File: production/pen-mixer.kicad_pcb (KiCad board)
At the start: 4 copper layers, 11 x 42 mm, 32 parts, among them J1 USB-C 16P, J2 BAT, J3 FSR, U1 ISP1807-LR, U2 LSM6DSV16X, U3 MCP73831T-2ACI/OT, U4 TPS7A0233DQN

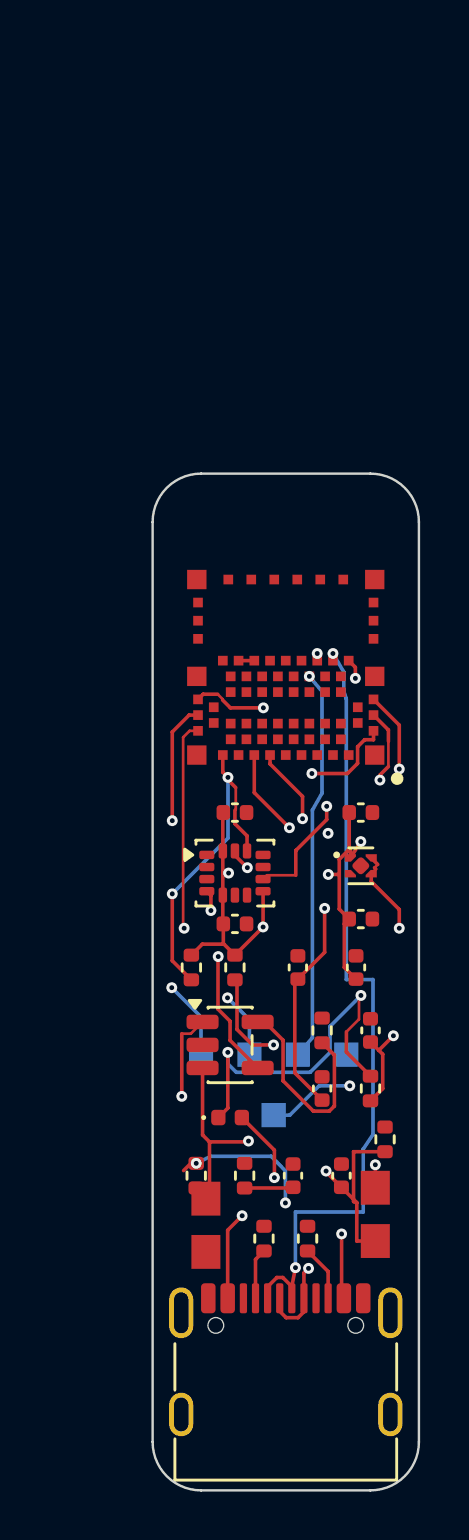
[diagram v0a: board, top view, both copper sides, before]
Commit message: vendor footprint full track routing
Claude-Session: https://claude.ai/code/session_01RCYT2QSY7BVZDeTyE9KrC4
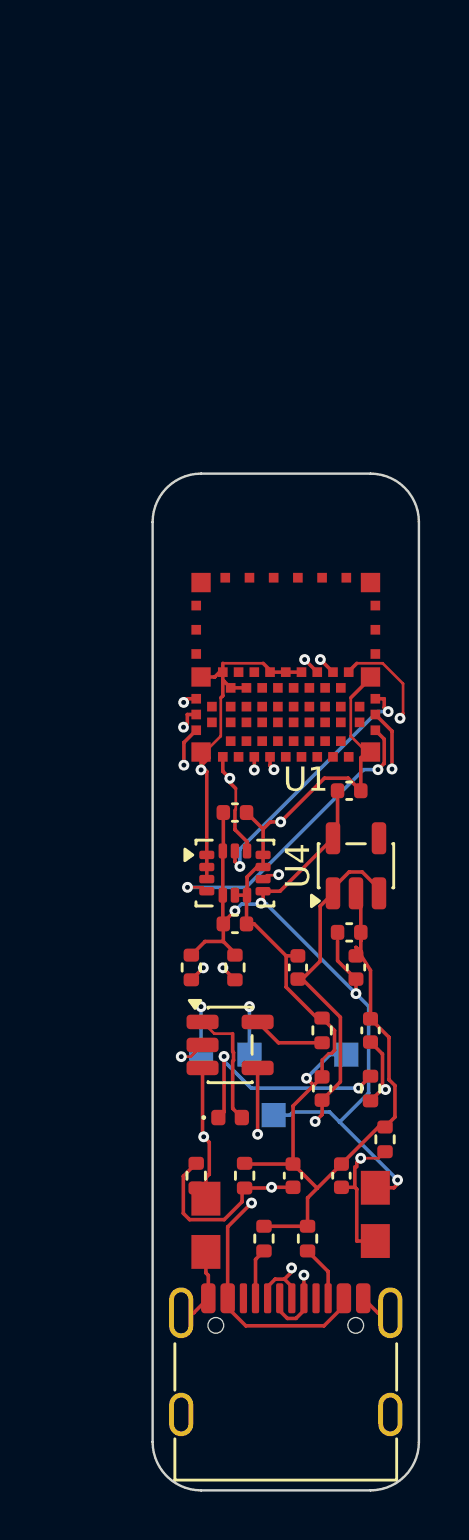
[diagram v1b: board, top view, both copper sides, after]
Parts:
- removed TP3: nRESET, TestPad_1.0mm
- U1: footprint ISP1807_LGA78_8x8mm -> ISP1807-LR
- U4: value TPS7A0233DQN -> TPS7A0533PDBV; footprint Texas_X2SON-4_1x1mm_P0.65mm -> SOT-23-5
- moved U1 5.66 mm to (109.5, 72.0)
- moved C5 1.02 mm to (108.1, 73.1)
- moved C6 0.73 mm to (108.1, 79.0)
- moved U4 0.20 mm to (108.4, 76.2), turned to 90 degrees
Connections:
- U1 pad 13: nRESET -> (no net)
- U1 pad 20: ANT -> (no net)
- U1 pad 22: ANT -> (no net)
- U4 pad 1: +3V3 -> VBAT
- U4 pad 4: VBAT -> (no net)
- U4 pad 5: GND -> +3V3
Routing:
- net GND: track 0.00 -> 112.4 mm, vias 1 -> 4
- net +3V3: track 27.8 -> 49.8 mm, vias 7 -> 5
- net nRESET: track 16.1 -> 0.00 mm, vias 1 -> 0
- net VBAT_SENSE: track 12.6 -> 25.8 mm, vias 3 -> 2
- net VBAT: track 34.5 -> 24.9 mm, vias 3 -> 2
- net VBUS: track 57.1 -> 48.7 mm, vias 5 -> 4
- net SCL: track 24.1 -> 16.2 mm
- net CHG_STAT: track 11.9 -> 5.10 mm, vias 2 -> 0
- net IPROG: track 8.59 -> 3.02 mm
- net LED_A: track 15.0 -> 9.53 mm
- net USB_DM: track 32.9 -> 29.3 mm
- net USB_DP: track 29.6 -> 32.1 mm
- net FSR_SENSE: track 27.9 -> 25.9 mm
- net IMU_INT2: track 10.5 -> 9.75 mm
- net SDA: track 14.0 -> 13.3 mm
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
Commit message: stock symbols full route zero unrouted
Claude-Session: https://claude.ai/code/session_01RCYT2QSY7BVZDeTyE9KrC4
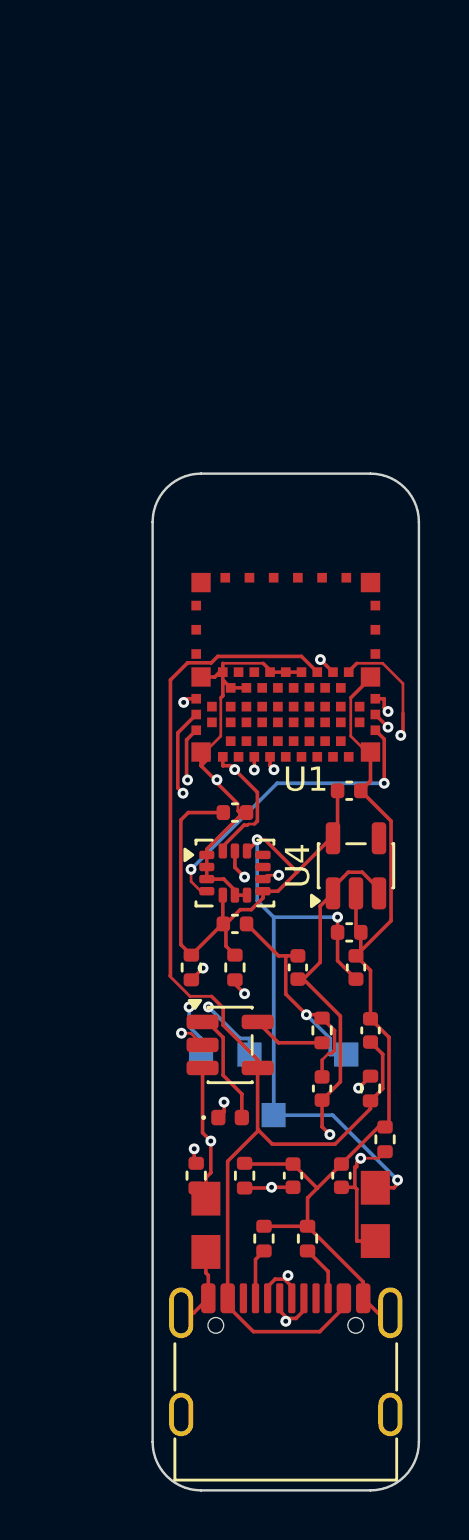
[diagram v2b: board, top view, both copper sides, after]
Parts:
- U2: value LSM6DSV16X -> LSM6DS3TR-C
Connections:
- U2 pad 10: GND -> (no net)
- U2 pad 11: GND -> (no net)
- U2 pad 12: SDA -> +3V3
- U2 pad 14: +3V3 -> SDA
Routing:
- net GND: track 112.4 -> 120.0 mm, vias 4 -> 3
- net +3V3: track 49.8 -> 55.9 mm, vias 5 -> 4
- net LED_A: track 9.53 -> 7.23 mm
- net VBAT_SENSE: track 25.8 -> 24.1 mm, vias 2 -> 3
- net SDA: track 13.3 -> 14.9 mm
- net USB_DP: track 32.1 -> 33.5 mm
- net VBUS: track 48.7 -> 49.8 mm, vias 4 -> 0
- net VBAT: track 24.9 -> 25.8 mm
- net SCL: track 16.2 -> 17.1 mm
- net SWDCLK: track 14.7 -> 15.3 mm

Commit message: remove fsr rearrange back pads
Claude-Session: https://claude.ai/code/session_01RCYT2QSY7BVZDeTyE9KrC4
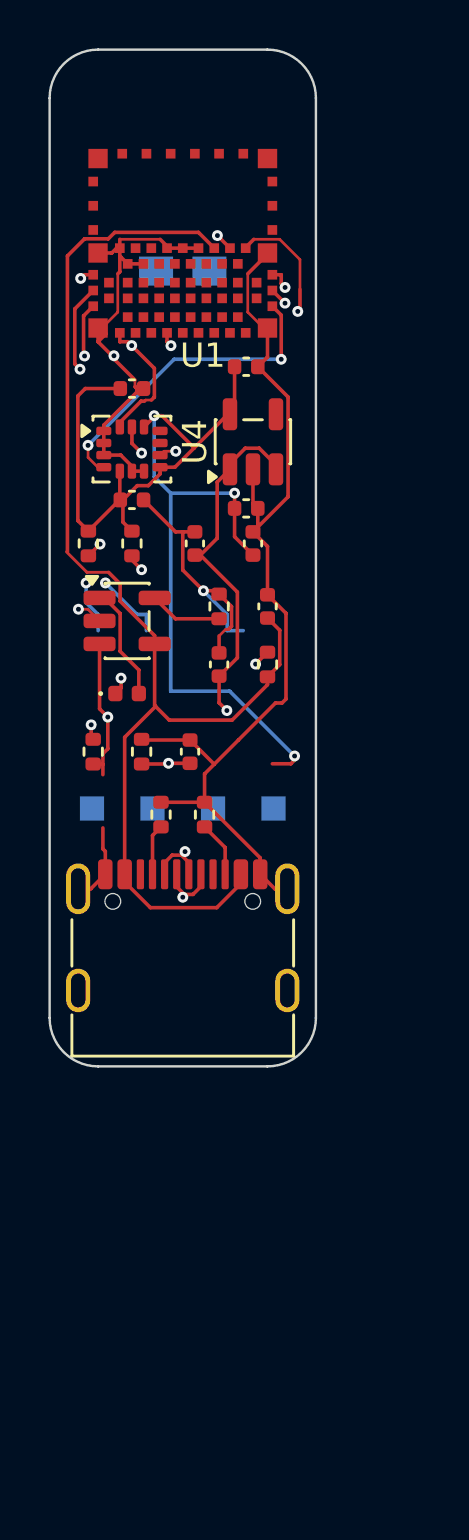
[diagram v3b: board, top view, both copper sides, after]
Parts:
- removed C9: 100n, C_0402_1005Metric
- removed J3: FSR, SolderPad_1.2x2.0mm
- removed R5: 10k, R_0402_1005Metric
- J2: moved to B.Cu
- moved J2 39.4 mm to (101.2, 51.6), turned to 90 degrees
- moved C2 18.0 mm to (102.7, 67.9)
- moved C3 18.0 mm to (101.7, 62.9)
- moved C4 18.0 mm to (104.1, 62.9)
- moved J1 18.0 mm to (101.2, 80.3)
- moved R4 18.0 mm to (104.7, 67.9)
- moved R7 18.0 mm to (99.1, 62.9)
- moved R6 18.0 mm to (97.3, 62.9)
- moved C6 18.0 mm to (103.9, 61.4)
- moved C7 18.0 mm to (99.1, 56.5)
- moved U1 18.0 mm to (105.2, 54.5)
- moved U2 18.0 mm to (99.1, 59.0)
- moved U4 18.0 mm to (104.1, 58.7)
- moved C1 18.0 mm to (104.7, 65.5)
- moved C10 18.0 mm to (101.5, 71.5)
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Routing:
- net FSR_SENSE: track 25.6 -> 0.00 mm, vias 2 -> 0

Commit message: swap tp and battery pad ends
Claude-Session: https://claude.ai/code/session_01RCYT2QSY7BVZDeTyE9KrC4
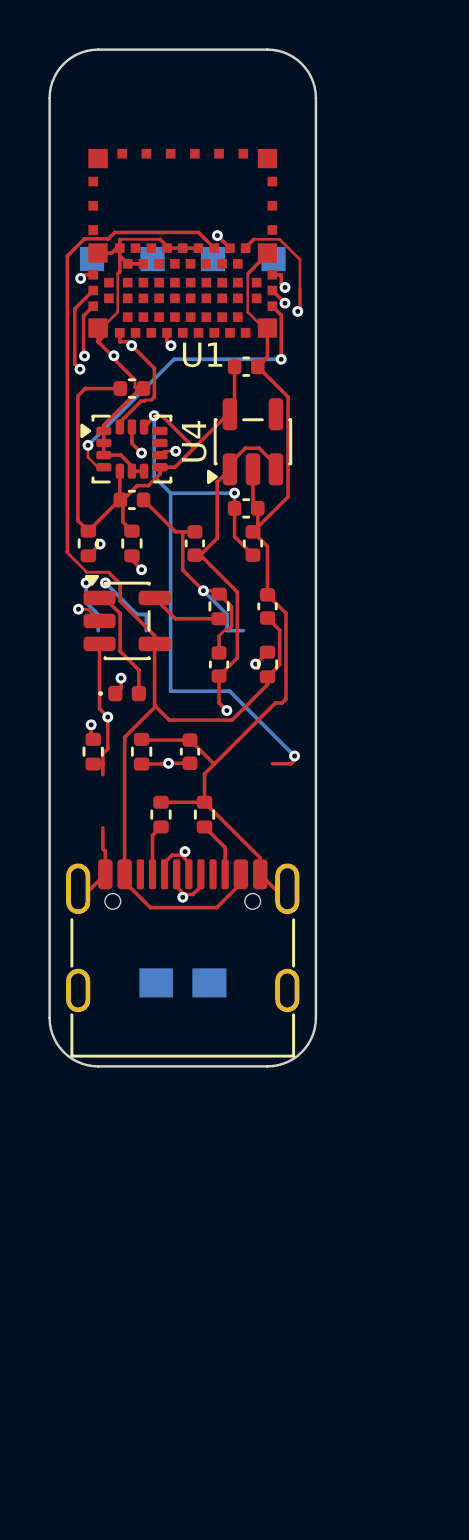
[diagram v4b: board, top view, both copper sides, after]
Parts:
- moved J2 29.4 mm to (101.2, 81.0)
- moved TP1 22.7 mm to (97.5, 51.1)
- moved TP2 22.7 mm to (100.0, 51.1)
- moved TP4 22.7 mm to (102.5, 51.1)
- moved TP5 22.7 mm to (105.0, 51.1)
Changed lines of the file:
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@@
 	(footprint "TestPad_1.0mm"
 		(layer "B.Cu")
-		(at 99.9952 73.8352)
+		(at 99.9952 51.1352)
 		(descr "1.0mm round-ish pogo test pad")
 		(property "Reference" "TP2"
@@
 	(footprint "TestPad_1.0mm"
 		(layer "B.Cu")
-		(at 104.9952 73.8352)
+		(at 104.9952 51.1352)
 		(descr "1.0mm round-ish pogo test pad")
 		(property "Reference" "TP5"
@@
 	(footprint "TestPad_1.0mm"
 		(layer "B.Cu")
-		(at 102.4952 73.8352)
+		(at 102.4952 51.1352)
 		(descr "1.0mm round-ish pogo test pad")
 		(property "Reference" "TP4"
@@
 	(footprint "SolderPad_1.2x2.0mm"
 		(layer "B.Cu")
-		(at 101.2452 51.6352 90)
+		(at 101.2452 81.0352 90)
 		(descr "Wire solder pad pair, 2.0mm pitch")
 		(property "Reference" "J2"
@@
 	(footprint "TestPad_1.0mm"
 		(layer "B.Cu")
-		(at 97.4952 73.8352)
+		(at 97.4952 51.1352)
 		(descr "1.0mm round-ish pogo test pad")
 		(property "Reference" "TP1"

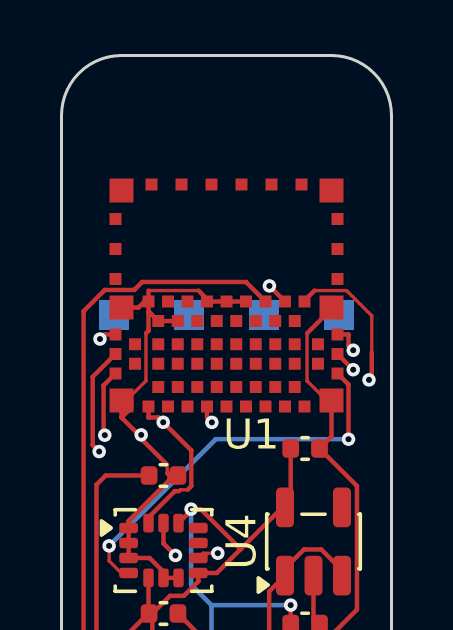
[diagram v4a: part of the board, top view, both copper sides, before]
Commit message: nudge tp1 clear of via
Claude-Session: https://claude.ai/code/session_01RCYT2QSY7BVZDeTyE9KrC4
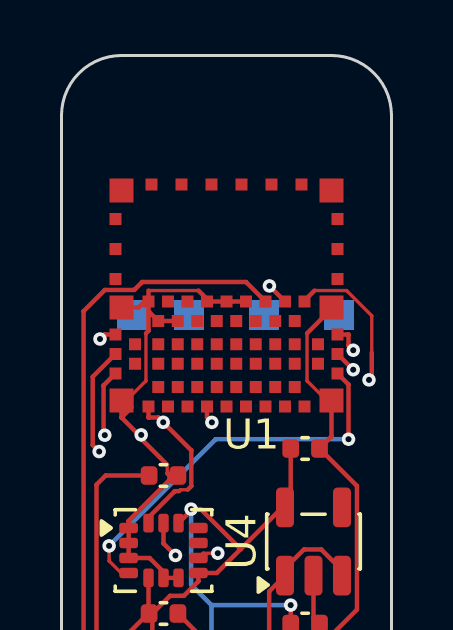
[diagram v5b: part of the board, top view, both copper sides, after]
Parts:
- moved TP1 0.60 mm to (98.1, 51.1)
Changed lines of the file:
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@@
 	(footprint "TestPad_1.0mm"
 		(layer "B.Cu")
-		(at 97.4952 51.1352)
+		(at 98.0952 51.1352)
 		(descr "1.0mm round-ish pogo test pad")
 		(property "Reference" "TP1"

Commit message: pads to board extremes
Claude-Session: https://claude.ai/code/session_01RCYT2QSY7BVZDeTyE9KrC4
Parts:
- moved J2 2.40 mm to (101.2, 83.4)
- moved TP5 1.49 mm to (103.9, 50.1)
- moved TP4 1.28 mm to (101.7, 50.1)
- moved TP1 1.08 mm to (97.7, 50.1)
- moved TP2 1.00 mm to (99.9, 50.1)
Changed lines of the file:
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@@
 	(footprint "TestPad_1.0mm"
 		(layer "B.Cu")
-		(at 99.9952 51.1352)
+		(at 99.8952 50.1352)
 		(descr "1.0mm round-ish pogo test pad")
 		(property "Reference" "TP2"
@@
 	(footprint "TestPad_1.0mm"
 		(layer "B.Cu")
-		(at 104.9952 51.1352)
+		(at 103.8952 50.1352)
 		(descr "1.0mm round-ish pogo test pad")
 		(property "Reference" "TP5"
@@
 	(footprint "TestPad_1.0mm"
 		(layer "B.Cu")
-		(at 102.4952 51.1352)
+		(at 101.6952 50.1352)
 		(descr "1.0mm round-ish pogo test pad")
 		(property "Reference" "TP4"
@@
 	(footprint "SolderPad_1.2x2.0mm"
 		(layer "B.Cu")
-		(at 101.2452 81.0352 90)
+		(at 101.2452 83.4352 90)
 		(descr "Wire solder pad pair, 2.0mm pitch")
 		(property "Reference" "J2"
@@
 	(footprint "TestPad_1.0mm"
 		(layer "B.Cu")
-		(at 98.0952 51.1352)
+		(at 97.6952 50.1352)
 		(descr "1.0mm round-ish pogo test pad")
 		(property "Reference" "TP1"

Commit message: test pads to board tip
Claude-Session: https://claude.ai/code/session_01RCYT2QSY7BVZDeTyE9KrC4
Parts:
- moved TP4 6.23 mm to (102.3, 43.9)
- moved TP5 6.23 mm to (104.5, 43.9)
- moved TP1 6.20 mm to (97.9, 43.9)
- moved TP2 6.20 mm to (100.1, 43.9)
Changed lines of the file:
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@@
 	(footprint "TestPad_1.0mm"
 		(layer "B.Cu")
-		(at 99.8952 50.1352)
+		(at 100.0952 43.9352)
 		(descr "1.0mm round-ish pogo test pad")
 		(property "Reference" "TP2"
@@
 	(footprint "TestPad_1.0mm"
 		(layer "B.Cu")
-		(at 103.8952 50.1352)
+		(at 104.4952 43.9352)
 		(descr "1.0mm round-ish pogo test pad")
 		(property "Reference" "TP5"
@@
 	(footprint "TestPad_1.0mm"
 		(layer "B.Cu")
-		(at 101.6952 50.1352)
+		(at 102.2952 43.9352)
 		(descr "1.0mm round-ish pogo test pad")
 		(property "Reference" "TP4"
@@
 	(footprint "TestPad_1.0mm"
 		(layer "B.Cu")
-		(at 97.6952 50.1352)
+		(at 97.8952 43.9352)
 		(descr "1.0mm round-ish pogo test pad")
 		(property "Reference" "TP1"

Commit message: route complete zero unrouted
Claude-Session: https://claude.ai/code/session_01RCYT2QSY7BVZDeTyE9KrC4
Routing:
- net GND: track 120.0 -> 142.5 mm, vias 3 -> 4
- net +3V3: track 55.9 -> 77.3 mm, vias 4 -> 5
- net SWDCLK: track 15.3 -> 30.5 mm
- net VBAT: track 25.8 -> 39.4 mm, vias 2 -> 3
- net SWDIO: track 15.1 -> 26.8 mm
